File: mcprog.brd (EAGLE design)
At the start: 160 x 100 mm, 53 parts, among them IC1 MCP2210SO, IC2 MCP1703SOT-89, J1 AVRSPI-61.27, J2 AVRSPI-62.56-V, Q1 MOSFET-NCHANNELSMD, X1 MICRO-USB-AB, X2 12MHz

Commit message: board, v1
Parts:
- moved Q1 266.4 mm to (12.5, 34.3), turned to 90 degrees
- moved R17 266.1 mm to (15.1, 34.2), turned to 270 degrees
- moved R14 257.8 mm to (15.5, 30.7), turned to 270 degrees
- moved Q3 252.2 mm to (12.7, 30.7), turned to 90 degrees
- moved R28 245.8 mm to (8.71, 33.5), turned to 180 degrees
- moved R11 238.3 mm to (10.4, 17.9)
- moved Q2 237.9 mm to (8.81, 30.5), turned to 180 degrees
- moved LED5 232.0 mm to (28.3, 34.5), turned to 90 degrees
- moved S1 226.8 mm to (3.19, 28.9), turned to 90 degrees
- moved JUMPER1 226.4 mm to (34.6, 2.23), turned to 180 degrees
- moved R26 225.6 mm to (28.4, 31.7), turned to 90 degrees
- moved LED4 223.8 mm to (24.4, 34.7), turned to 90 degrees
- moved R25 217.5 mm to (24.6, 31.9), turned to 90 degrees
- moved C9 198.2 mm to (10.3, 25.8)
- moved R24 197.8 mm to (31.9, 14.1), turned to 90 degrees
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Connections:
- removed net !RESET!: R3.1, R6.1, R8.1
- removed net !RST_UC!: IC1.5, R24.2
- new net !RST_TARGET!: IC1.5, R24.2, R3.1, R6.1, R8.1
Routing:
- net VDD: track 0.00 -> 82.5 mm, vias 0 -> 3
- net V_TARGET: track 0.00 -> 54.3 mm
- net MISO: track 0.00 -> 45.8 mm, vias 0 -> 3
- net SCK: track 0.00 -> 38.1 mm, vias 0 -> 2
- net +5V: track 0.00 -> 36.6 mm
- net +3V3: track 0.00 -> 30.8 mm
- net !RST_TARGET!: track 0.00 -> 26.7 mm, vias 0 -> 3
- net N$21: track 0.00 -> 22.7 mm
- net VUSB: track 0.00 -> 22.1 mm, vias 0 -> 2
- net N$33: track 0.00 -> 21.5 mm, vias 0 -> 2
- net MOSI: track 0.00 -> 20.4 mm
- net N$30: track 0.00 -> 19.4 mm, vias 0 -> 2
- net !USB_CFG!: track 0.00 -> 18.2 mm, vias 0 -> 2
- net N$20: track 0.00 -> 17.6 mm
- net N$25: track 0.00 -> 16.8 mm
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- added copper zone on layer 1, net GND
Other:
- board size 160 x 100 mm -> 45.8 x 37.2 mm
- board text added: "+3V3"
- board text added: "+5V"
- board text added: "1->"
- board text added: "ERROR"
- board text added: "PROG"
- board text added: "SUPPLY V_TARGET"
- board text added: "USB CFG"
- board text added: "V_TARGET"
- board text added: "mcprog"
- board text added: "www.bytewerk.org"

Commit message: v1.0
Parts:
- moved C6 12.9 mm to (8.84, 18.9)
- moved R28 9.13 mm to (15.9, 27.9), turned to 0 degrees
- moved R14 8.90 mm to (7.12, 27.7), turned to 90 degrees
- moved Q2 6.98 mm to (15.8, 30.7), turned to 0 degrees
- moved R17 5.22 mm to (10.3, 32.2), turned to 90 degrees
- moved Q3 4.68 mm to (8.08, 31.1), turned to 0 degrees
- moved R11 3.59 mm to (13.5, 19.6), turned to 90 degrees
- moved Q1 3.58 mm to (12.7, 30.7), turned to 180 degrees
- moved C7 1.41 mm to (14.8, 24.7)
- moved C8 1.20 mm to (14.5, 22.3)
- moved LOGO1 1.08 mm to (4.25, 2.55)
- moved LED2 0.89 mm to (31.2, 34.3)
- moved C9 0.82 mm to (9.50, 25.6)
- moved R18 0.80 mm to (31.3, 31.7)
- moved R26 0.63 mm to (27.8, 31.9)
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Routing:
- net +5V: track 36.6 -> 26.4 mm
- net GND: track 0.00 -> 8.37 mm, vias 0 -> 2
- net V_TARGET: track 54.3 -> 61.3 mm
- net VDD: track 82.5 -> 89.3 mm, vias 3 -> 2
- net N$24: track 5.68 -> 10.0 mm
- net +3V3: track 30.8 -> 33.5 mm
- net VUSB: track 22.1 -> 24.1 mm
- net N$11: track 5.37 -> 6.94 mm
- net N$33: track 21.5 -> 20.1 mm
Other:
- board text added: "v1.0"

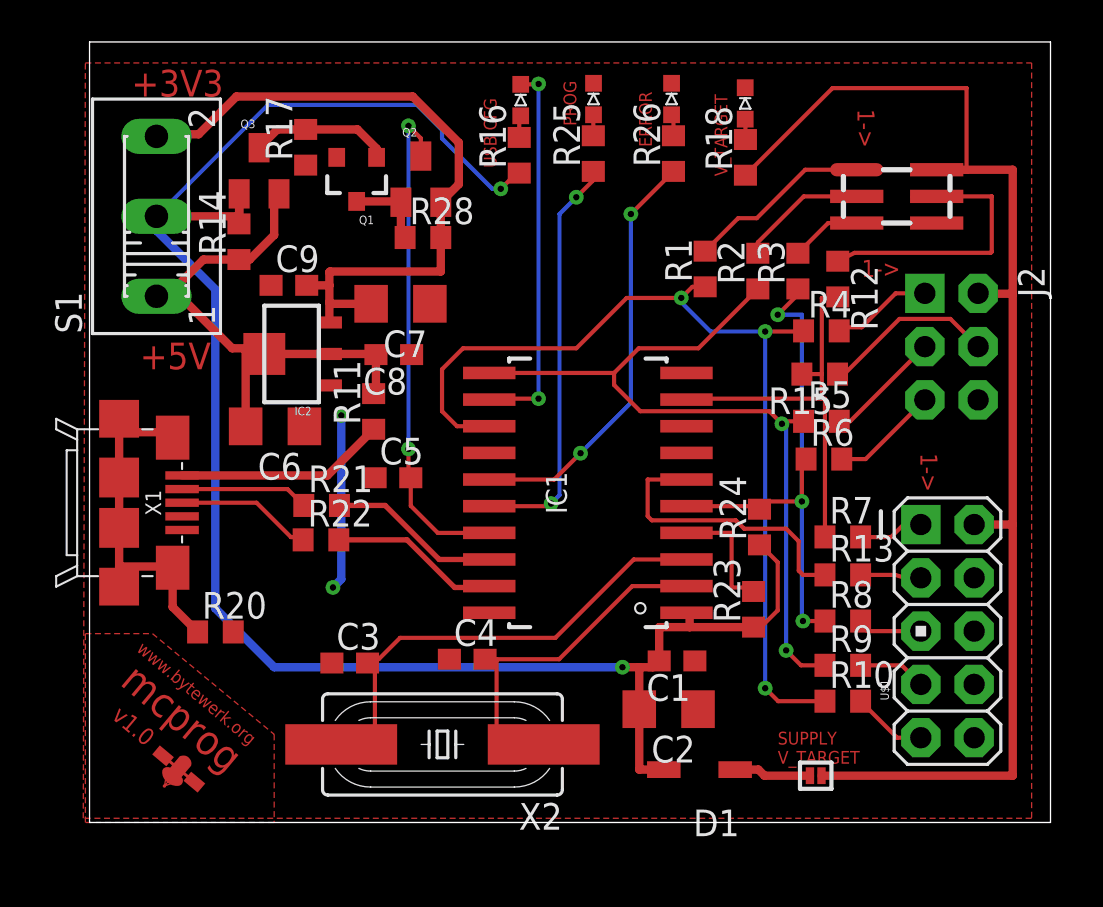
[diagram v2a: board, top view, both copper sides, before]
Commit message: Fixing some minor DRC problems. R23 now is 10k
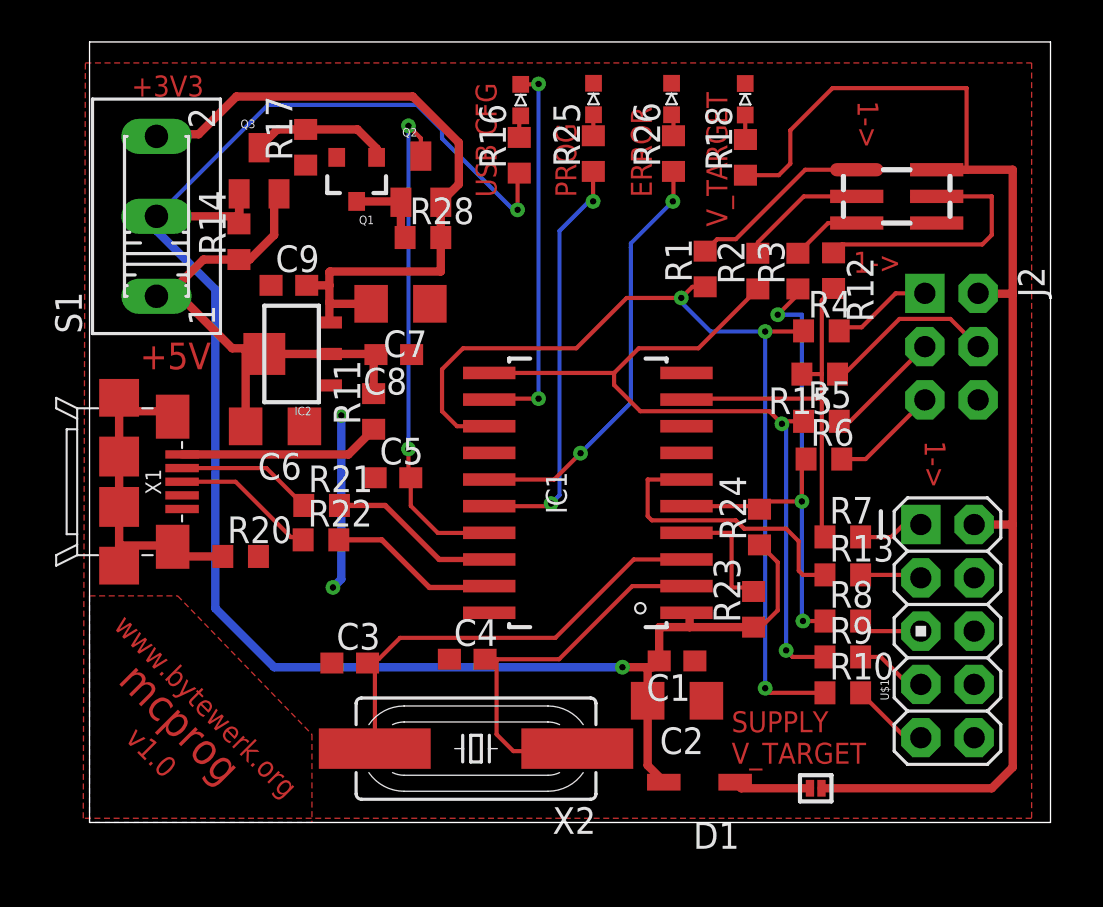
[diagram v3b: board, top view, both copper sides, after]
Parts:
- removed LOGO1: (no value), bytewerk-logo:BYTEWERK-LOGO
- R23: value 1k -> 10k
- moved R20 3.79 mm to (7.20, 12.7)
- moved X2 1.61 mm to (18.4, 3.52)
- moved X1 1.00 mm to (1.41, 16.2)
- moved D1 0.60 mm to (29.1, 1.92)
- moved JUMPER1 0.60 mm to (34.6, 1.63)
- moved C2 0.57 mm to (28.0, 5.80)
- moved R12 0.45 mm to (35.5, 26.3)
- moved R10 0.40 mm to (35.9, 6.18)
- moved R9 0.40 mm to (35.9, 7.89)
- moved LED2 0.20 mm to (31.2, 34.5)
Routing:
- net VDD: track 89.3 -> 91.0 mm
- net N$20: track 17.6 -> 18.9 mm
- net N$21: track 22.7 -> 21.5 mm
- net N$25: track 16.8 -> 15.8 mm
- net V_TARGET: track 61.3 -> 62.2 mm
- net MOSI: track 20.4 -> 19.6 mm

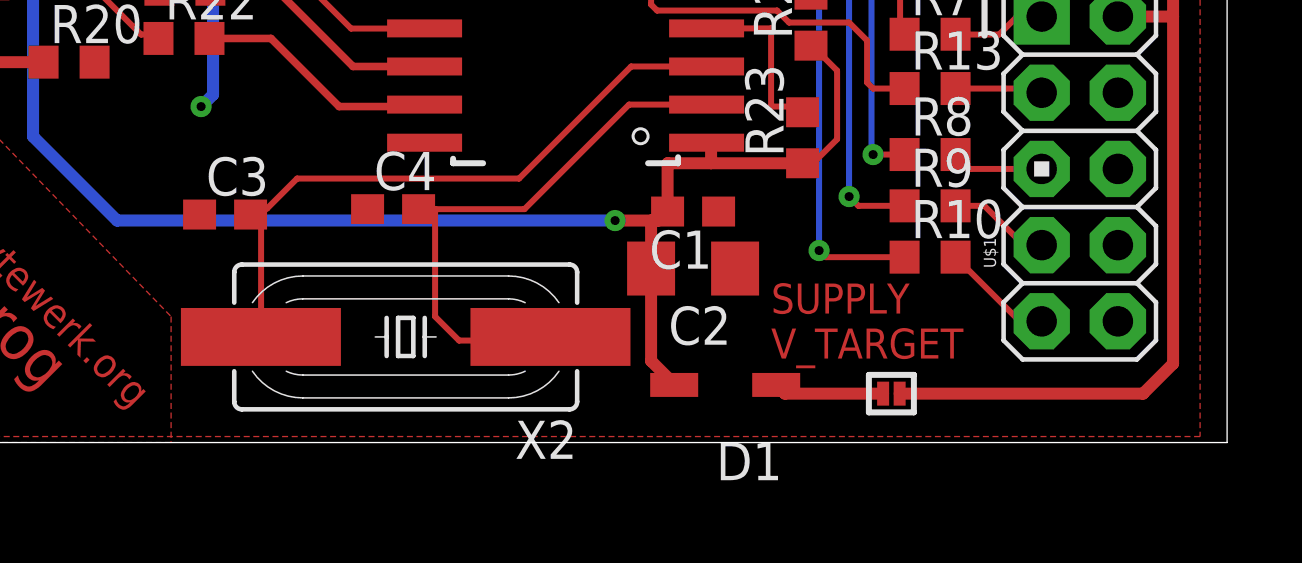
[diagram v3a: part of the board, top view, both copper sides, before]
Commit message: improve GND path
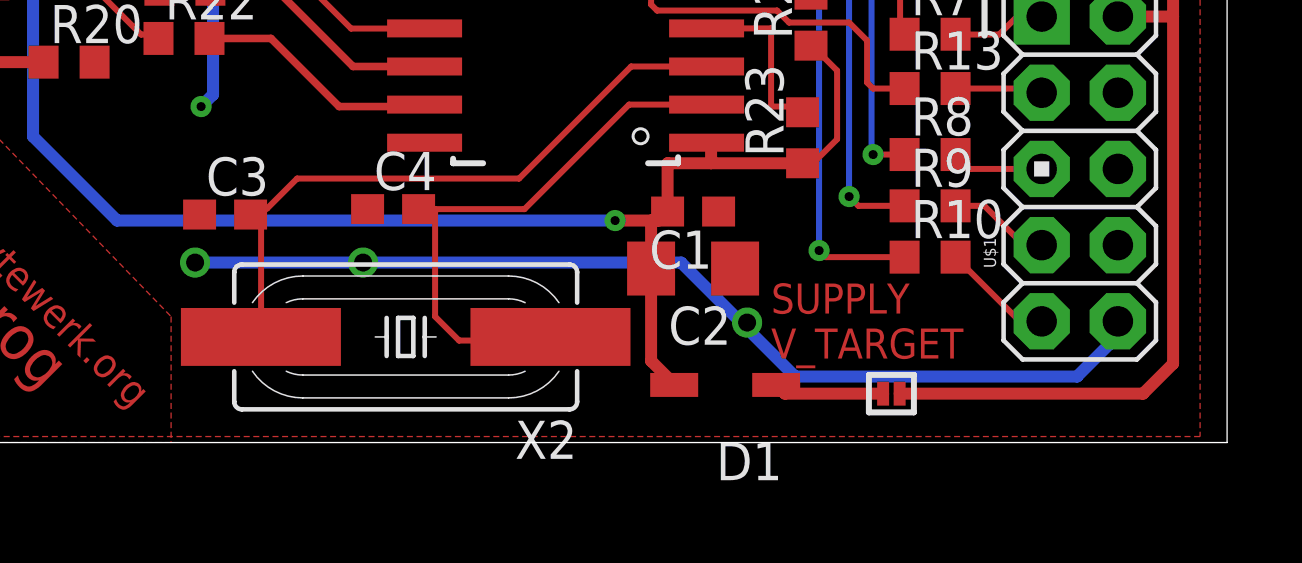
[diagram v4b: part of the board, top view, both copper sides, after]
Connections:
- net GND: no longer U$1.4, U$1.6, U$1.8
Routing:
- net GND: track 8.37 -> 41.7 mm, vias 2 -> 5
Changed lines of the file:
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@@
 <contactref element="J1" pad="6"/>
 <contactref element="J2" pad="6"/>
-<contactref element="U$1" pad="4"/>
-<contactref element="U$1" pad="10"/>
-<contactref element="U$1" pad="8"/>
-<contactref element="U$1" pad="6"/>
 <contactref element="X1" pad="5"/>
 <contactref element="R20" pad="2"/>
@@
 <vertex x="0" y="0"/>
 </polygon>
+<via x="11.4" y="6" extent="1-16" drill="0.6"/>
+<wire x1="40.8" y1="2.2" x2="42.2" y2="3.6" width="0.4" layer="16"/>
+<wire x1="42.2" y1="3.6" x2="42.2" y2="4" width="0.4" layer="16"/>
+<contactref element="U$1" pad="10"/>
+<wire x1="11.4" y1="6" x2="17" y2="6" width="0.4" layer="16"/>
+<wire x1="17" y1="6" x2="27.6" y2="6" width="0.4" layer="16"/>
+<wire x1="27.6" y1="6" x2="31.4" y2="2.2" width="0.4" layer="16"/>
+<wire x1="31.4" y1="2.2" x2="40.8" y2="2.2" width="0.4" layer="16"/>
+<via x="17" y="6" extent="1-16" drill="0.6"/>
+<via x="29.8" y="4" extent="1-16" drill="0.6"/>
 </signal>
 <signal name="MOSI">
